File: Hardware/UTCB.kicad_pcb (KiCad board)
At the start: 2 copper layers, 193 parts, among them J1 NR01105ANG13-2C, J10 Conn_01x06, J2 NR01105ANG13-2C, J3 NR01105ANG13-2C, J4 NR01105ANG13-2C, J5 NR01105ANG13-2C, J6 NR01105ANG13-2C, J7 VXO7805-500-M-TR, J8 3557-2, J9 Conn_01x02, Q1 2SD2653KT146, Q10 2SD2653KT146, Q11 2SD2653KT146, Q12 2SD2653KT146, Q13 2SD2653KT146, Q14 2SD2653KT146, Q15 2SD2653KT146, Q16 2SD2653KT146, Q17 2SD2653KT146, Q18 2SD2653KT146, Q19 2SD2653KT146, Q2 2SD2653KT146, Q20 2SD2653KT146, Q21 2SD2653KT146, Q22 2SD2653KT146, Q23 2SD2653KT146, Q24 2SD2653KT146, Q25 2SD2653KT146, Q26 2SD2653KT146, Q27 2SD2653KT146, Q28 2SD2653KT146, Q29 2SD2653KT146, Q3 2SD2653KT146, Q30 2SD2653KT146, Q31 2SD2653KT146, Q32 2SD2653KT146, Q33 2SD2653KT146, Q34 2SD2653KT146, Q35 2SD2653KT146, Q36 2SD2653KT146, Q37 2SD2653KT146, Q38 2SD2653KT146, Q39 2SD2653KT146, Q4 2SD2653KT146, Q40 2SD2653KT146, Q41 2SD2653KT146, Q42 2SD2653KT146, Q43 2SD2653KT146, Q44 2SD2653KT146, Q45 2SD2653KT146, Q46 2SD2653KT146, Q47 2SD2653KT146, Q48 2SD2653KT146, Q5 2SD2653KT146, Q6 2SD2653KT146, Q7 2SD2653KT146, Q8 2SD2653KT146, Q9 2SD2653KT146

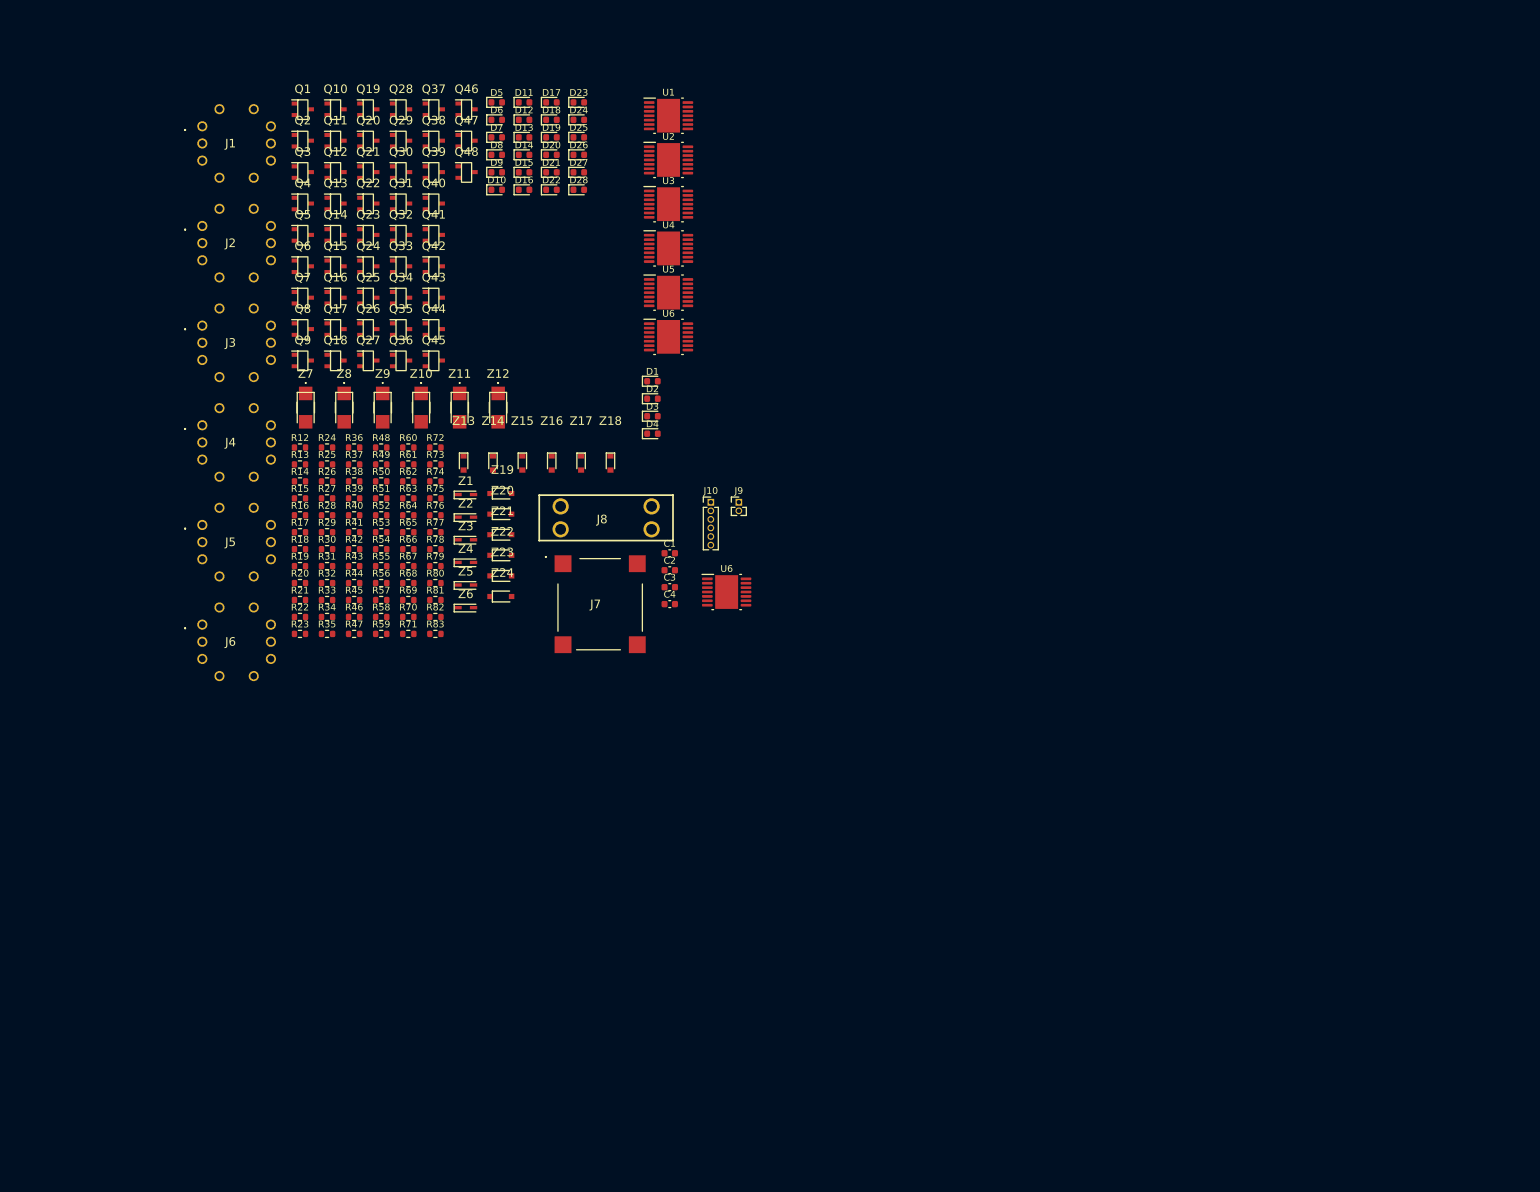
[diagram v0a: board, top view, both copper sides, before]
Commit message: Added updates to logic switches for timing based logic. Updated attached 3D models.
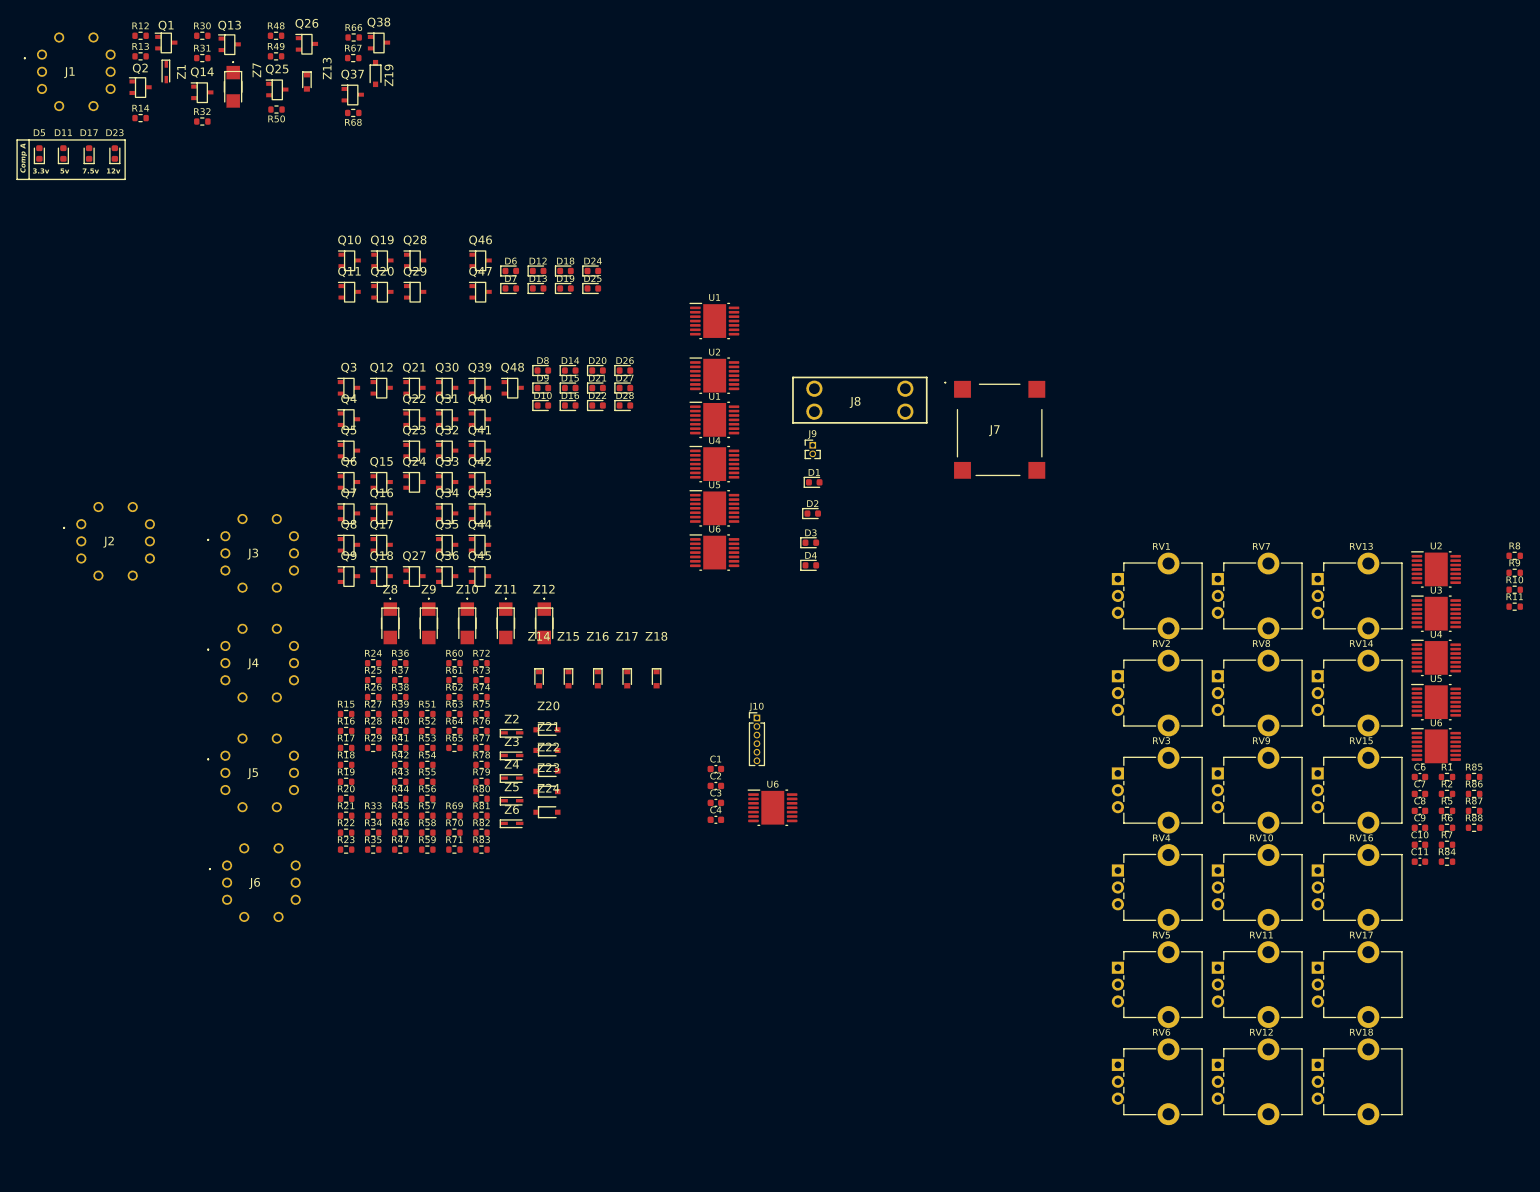
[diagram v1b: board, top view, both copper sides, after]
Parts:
- added C10: 10uF, Capacitor_SMD:C_0603_1608Metric, F.Cu at (223.5, 135.0)
- added C11: 10uF, Capacitor_SMD:C_0603_1608Metric, F.Cu at (223.5, 137.6)
- added C6: 10uF, Capacitor_SMD:C_0603_1608Metric, F.Cu at (223.5, 125.0)
- added C7: 10uF, Capacitor_SMD:C_0603_1608Metric, F.Cu at (223.5, 127.5)
- added C8: 10uF, Capacitor_SMD:C_0603_1608Metric, F.Cu at (223.5, 130.0)
- added C9: 10uF, Capacitor_SMD:C_0603_1608Metric, F.Cu at (223.5, 132.5)
- added R1: 10kΩ, Resistor_SMD:R_0603_1608Metric, F.Cu at (227.5, 125.0)
- added R10: R_Small, Resistor_SMD:R_0603_1608Metric, F.Cu at (237.5, 97.3)
- added R11: R_Small, Resistor_SMD:R_0603_1608Metric, F.Cu at (237.5, 99.8)
- added R2: 10kΩ, Resistor_SMD:R_0603_1608Metric, F.Cu at (227.5, 127.5)
- added R5: 10kΩ, Resistor_SMD:R_0603_1608Metric, F.Cu at (227.5, 130.0)
- added R6: 10kΩ, Resistor_SMD:R_0603_1608Metric, F.Cu at (227.5, 132.5)
- added R7: 10kΩ, Resistor_SMD:R_0603_1608Metric, F.Cu at (227.5, 135.0)
- added R8: R_Small, Resistor_SMD:R_0603_1608Metric, F.Cu at (237.5, 92.3)
- added R84: 10kΩ, Resistor_SMD:R_0603_1608Metric, F.Cu at (227.5, 137.6)
- added R85: 10kΩ, Resistor_SMD:R_0603_1608Metric, F.Cu at (231.5, 125.0)
- added R86: 10kΩ, Resistor_SMD:R_0603_1608Metric, F.Cu at (231.5, 127.5)
- added R87: 10kΩ, Resistor_SMD:R_0603_1608Metric, F.Cu at (231.5, 130.0)
- added R88: 10kΩ, Resistor_SMD:R_0603_1608Metric, F.Cu at (231.5, 132.5)
- added R9: R_Small, Resistor_SMD:R_0603_1608Metric, F.Cu at (237.5, 94.8)
- added RV1: R_Potentiometer_Trim, Potentiometer_THT:Potentiometer_Alpha_RD901F-40-00D_Single_Vertical_CircularHoles, F.Cu at (178.8, 95.7)
- added RV10: R_Potentiometer_Trim, Potentiometer_THT:Potentiometer_Alpha_RD901F-40-00D_Single_Vertical_CircularHoles, F.Cu at (193.6, 138.9)
- added RV11: 10kΩ, Potentiometer_THT:Potentiometer_Alpha_RD901F-40-00D_Single_Vertical_CircularHoles, F.Cu at (193.6, 153.3)
- added RV12: R_Potentiometer_Trim, Potentiometer_THT:Potentiometer_Alpha_RD901F-40-00D_Single_Vertical_CircularHoles, F.Cu at (193.6, 167.6)
- added RV13: 10kΩ, Potentiometer_THT:Potentiometer_Alpha_RD901F-40-00D_Single_Vertical_CircularHoles, F.Cu at (208.4, 95.7)
- added RV14: R_Potentiometer_Trim, Potentiometer_THT:Potentiometer_Alpha_RD901F-40-00D_Single_Vertical_CircularHoles, F.Cu at (208.4, 110.1)
- added RV15: 10kΩ, Potentiometer_THT:Potentiometer_Alpha_RD901F-40-00D_Single_Vertical_CircularHoles, F.Cu at (208.4, 124.5)
- added RV16: R_Potentiometer_Trim, Potentiometer_THT:Potentiometer_Alpha_RD901F-40-00D_Single_Vertical_CircularHoles, F.Cu at (208.4, 138.9)
- added RV17: R_Potentiometer_Trim, Potentiometer_THT:Potentiometer_Alpha_RD901F-40-00D_Single_Vertical_CircularHoles, F.Cu at (208.4, 153.3)
- added RV18: R_Potentiometer_Trim, Potentiometer_THT:Potentiometer_Alpha_RD901F-40-00D_Single_Vertical_CircularHoles, F.Cu at (208.4, 167.6)
- added RV2: R_Potentiometer_Trim, Potentiometer_THT:Potentiometer_Alpha_RD901F-40-00D_Single_Vertical_CircularHoles, F.Cu at (178.8, 110.1)
- added RV3: 10kΩ, Potentiometer_THT:Potentiometer_Alpha_RD901F-40-00D_Single_Vertical_CircularHoles, F.Cu at (178.8, 124.5)
- added RV4: R_Potentiometer_Trim, Potentiometer_THT:Potentiometer_Alpha_RD901F-40-00D_Single_Vertical_CircularHoles, F.Cu at (178.8, 138.9)
- added RV5: 10kΩ, Potentiometer_THT:Potentiometer_Alpha_RD901F-40-00D_Single_Vertical_CircularHoles, F.Cu at (178.8, 153.3)
- added RV6: R_Potentiometer_Trim, Potentiometer_THT:Potentiometer_Alpha_RD901F-40-00D_Single_Vertical_CircularHoles, F.Cu at (178.8, 167.6)
- added RV7: R_Potentiometer_Trim, Potentiometer_THT:Potentiometer_Alpha_RD901F-40-00D_Single_Vertical_CircularHoles, F.Cu at (193.6, 95.7)
- added RV8: 10kΩ, Potentiometer_THT:Potentiometer_Alpha_RD901F-40-00D_Single_Vertical_CircularHoles, F.Cu at (193.6, 110.1)
- added RV9: R_Potentiometer_Trim, Potentiometer_THT:Potentiometer_Alpha_RD901F-40-00D_Single_Vertical_CircularHoles, F.Cu at (193.6, 124.5)
- added U2: ~, Package_SO:HTSSOP-14-1EP_4.4x5mm_P0.65mm_EP3.4x5mm_Mask3x3.1mm, F.Cu at (225.9, 94.3)
- added U3: ~, Package_SO:HTSSOP-14-1EP_4.4x5mm_P0.65mm_EP3.4x5mm_Mask3x3.1mm, F.Cu at (225.9, 100.8)
- added U4: ~, Package_SO:HTSSOP-14-1EP_4.4x5mm_P0.65mm_EP3.4x5mm_Mask3x3.1mm, F.Cu at (225.9, 107.4)
- added U5: ~, Package_SO:HTSSOP-14-1EP_4.4x5mm_P0.65mm_EP3.4x5mm_Mask3x3.1mm, F.Cu at (225.9, 113.9)
- added U6: ~, Package_SO:HTSSOP-14-1EP_4.4x5mm_P0.65mm_EP3.4x5mm_Mask3x3.1mm, F.Cu at (225.9, 120.5)
- moved R30 78.2 mm to (43.2, 15.2)
- moved R31 77.5 mm to (43.2, 18.5)
- moved Z1 76.7 mm to (37.8, 20.6), turned to -90 degrees
- moved R66 76.2 mm to (65.6, 15.5)
- moved R67 75.7 mm to (65.5, 18.5)
- moved R32 70.8 mm to (43.2, 27.9)
- moved R68 70.1 mm to (65.5, 26.7), turned to 180 degrees
- moved D23 69.1 mm to (30.2, 32.7), turned to 90 degrees
- moved D17 68.9 mm to (26.4, 32.7), turned to 90 degrees
- moved D11 68.6 mm to (22.6, 32.7), turned to 90 degrees
- moved D5 68.2 mm to (19.1, 32.7), turned to 90 degrees
- moved R12 65.4 mm to (34.0, 15.2)
- moved Z19 64.9 mm to (68.8, 20.8), turned to -90 degrees
- moved R13 64.9 mm to (34.0, 18.3)
- moved J7 64.6 mm to (161.3, 73.6)
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- renumbered U3 to U1
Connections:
- U1 pad 10: unconnected-(U3-4IN--Pad10) -> unconnected-(U1-4IN--Pad10)
- U1 pad 11: unconnected-(U3-4IN+-Pad11) -> unconnected-(U1-4IN+-Pad11)
- U1 pad 4: unconnected-(U3-1IN--Pad4) -> Signal1
- U1 pad 5: unconnected-(U3-1IN+-Pad5) -> /ComparatorLogic/COMP1_HIGH
- U1 pad 6: unconnected-(U3-2IN--Pad6) -> /ComparatorLogic/COMP1_LOW
- U1 pad 7: unconnected-(U3-2IN+-Pad7) -> Signal1
- U1 pad 8: unconnected-(U3-3IN+-Pad8) -> /ComparatorLogic/Timing1Check
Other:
- board text added: "12v"
- board text added: "3.3v"
- board text added: "5v"
- board text added: "7.5v"
- board text added: "Comp A"

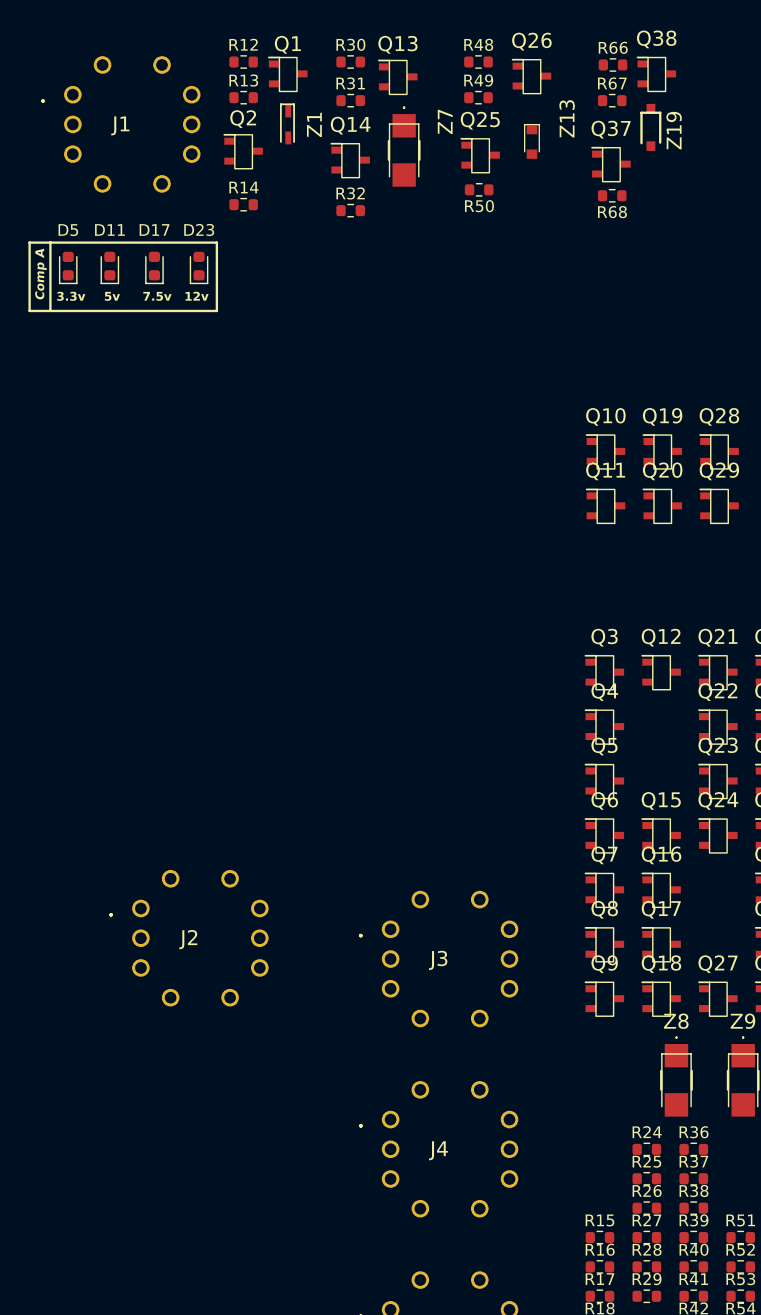
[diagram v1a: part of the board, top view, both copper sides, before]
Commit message: Added changes to logic timing
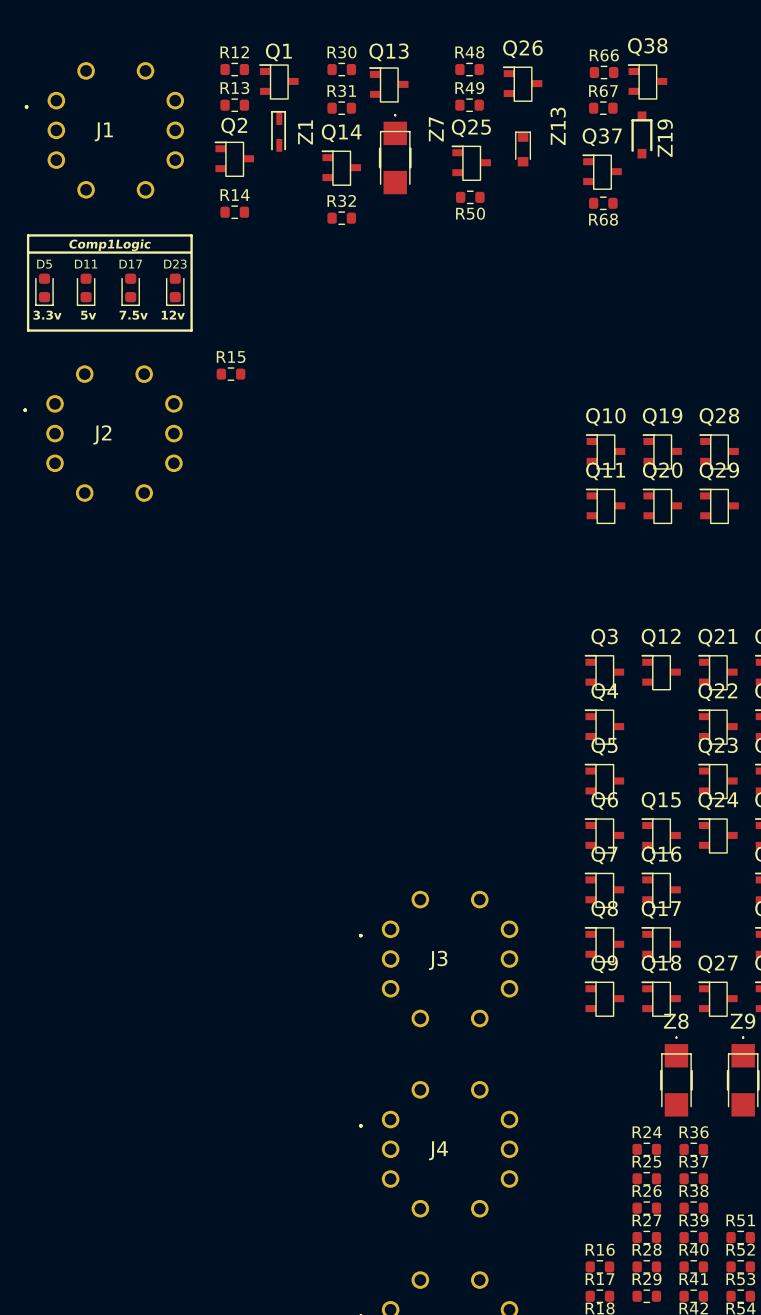
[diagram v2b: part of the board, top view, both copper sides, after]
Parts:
- moved R15 80.2 mm to (33.0, 41.9)
- moved J2 43.7 mm to (17.9, 44.5)
- moved D11 2.76 mm to (20.6, 34.5)
- moved D17 2.76 mm to (24.4, 34.5)
- moved D23 2.76 mm to (28.2, 34.5)
- moved D5 2.76 mm to (17.0, 34.5)
- moved J1 1.50 mm to (18.0, 18.5)
- moved Q2 1.00 mm to (33.3, 23.5)
- moved Q37 1.00 mm to (64.7, 24.6)
- moved R14 1.00 mm to (33.3, 28.1)
- moved R50 1.00 mm to (53.4, 26.8)
- moved R66 1.00 mm to (64.8, 16.1)
- moved Z13 1.00 mm to (57.9, 22.2)
- moved Z19 1.00 mm to (68.1, 21.5)
- moved R12 1.00 mm to (33.3, 15.9)
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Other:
- board text added: "Comp1Logic"
- board text removed: "Comp A"
